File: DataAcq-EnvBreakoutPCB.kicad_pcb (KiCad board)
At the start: 2 copper layers, 19 x 41.3 mm, 22 parts, among them J1 Airflow, J2 Temp, J3 Humidity, U1 FS3000-1005, U2 LMT87DCK, U3 SHT45

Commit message: tweaking
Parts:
- removed J1: Airflow, Connector_Molex:Molex_Nano-Fit_105309-xx04_1x04_P2.50mm_Vertical
- removed J2: Temp, Connector_Molex:Molex_Nano-Fit_105309-xx03_1x03_P2.50mm_Vertical
- removed J3: Humidity, Connector_Molex:Molex_Nano-Fit_105309-xx04_1x04_P2.50mm_Vertical
- added J4: Breakout Connector, Connector_Molex:Molex_Nano-Fit_105310-xx10_2x05_P2.50mm_Vertical, B.Cu at (128.4, 38.6)
- C5, C6, R1: moved to B.Cu
- LOGO3: footprint UTSVT_Special:UTSVT_Logo_Symbol -> images:utsvt_small; moved to B.Cu
- moved LOGO3 36.3 mm to (115.8, 29.9)
- moved LOGO1 16.9 mm to (116.0, 45.4), turned to 180 degrees
- moved D2 11.7 mm to (127.2, 32.8)
- moved R3 11.7 mm to (129.5, 32.9)
- moved C3 10.3 mm to (122.4, 33.9), turned to 0 degrees
- moved C2 10.1 mm to (115.7, 33.9), turned to 0 degrees
- moved C1 7.09 mm to (117.3, 38.0), turned to -90 degrees
- moved C4 6.70 mm to (119.6, 38.0), turned to 90 degrees
- moved R2 6.62 mm to (127.2, 54.5)
- moved D1 6.62 mm to (129.4, 54.5)
- moved C6 6.53 mm to (122.4, 49.6)
- moved R1 6.53 mm to (120.2, 49.6)
- moved C5 4.88 mm to (124.2, 53.2), turned to 90 degrees
- moved H2 3.35 mm to (121.5, 29.6)
- moved C7 3.16 mm to (119.2, 44.6), turned to 90 degrees
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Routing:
- net /I2C2_SCL: track 14.2 -> 6.41 mm
- net /PA1(ADC): track 15.5 -> 9.30 mm, vias 1 -> 0
- net /I2C2_SDA: track 12.4 -> 7.48 mm, vias 1 -> 0
- net /TEMP_OUT: track 4.99 -> 2.05 mm, vias 0 -> 1
- net GNDA: track 19.5 -> 16.6 mm, vias 1 -> 2
- net Net-(D2-A): track 2.27 -> 0.00 mm
- net Net-(D1-A): track 2.26 -> 0.00 mm
- net /I2C1_SCL: track 8.22 -> 6.82 mm
- net +3.3V: track 0.00 -> 1.35 mm, vias 1 -> 2
- net /I2C1_SDA: track 9.25 -> 8.37 mm, vias 0 -> 1
- net VDDA: track 13.9 -> 14.7 mm
- net GND: vias 5 -> 4
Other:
- board size 19 x 41.3 mm -> 18.7 x 35.2 mm
- board text added: "EnvBrd Conn"
- board text removed: "Aflw"
- board text removed: "Hmdty"

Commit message: im blind
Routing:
- net Net-(D2-A): track 0.00 -> 2.27 mm
- net Net-(D1-A): track 0.00 -> 2.26 mm
- net GND: vias 4 -> 5
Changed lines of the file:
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@@
+	)
+	(via
+		(at 127.25 33.7675)
+		(size 0.6)
+		(drill 0.3)
+		(layers "F.Cu" "B.Cu")
+		(net 2)
 	)
 	(via
@@
 	)
 	(segment
+		(start 127.225 55.45)
+		(end 127.2 55.425)
+		(width 0.2)
+		(layer "B.Cu")
+		(net 10)
+	)
+	(segment
+		(start 129.45 55.45)
+		(end 127.225 55.45)
+		(width 0.2)
+		(layer "B.Cu")
+		(net 10)
+	)
+	(segment
+		(start 127.295 31.9375)
+		(end 127.25 31.8925)
+		(width 0.2)
+		(layer "B.Cu")
+		(net 11)
+	)
+	(segment
+		(start 129.5 31.9375)
+		(end 127.295 31.9375)
+		(width 0.2)
+		(layer "B.Cu")
+		(net 11)
+	)
+	(segment

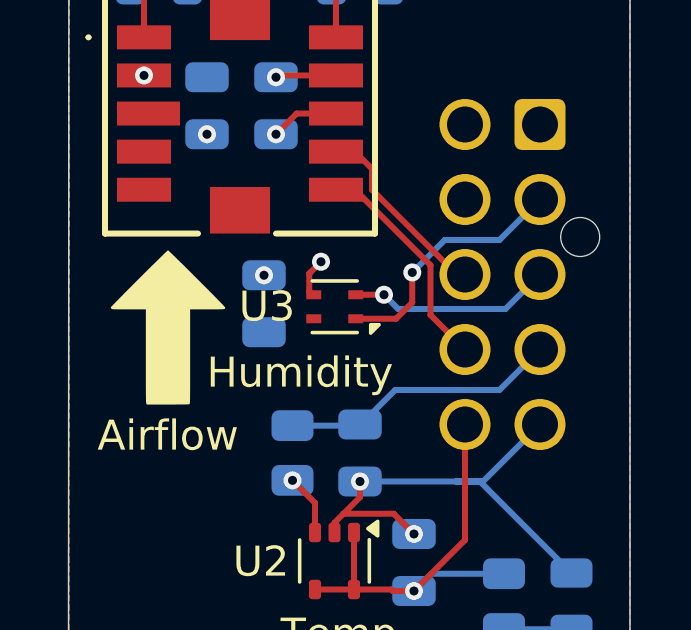
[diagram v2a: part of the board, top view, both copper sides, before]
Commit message: rearrange connector
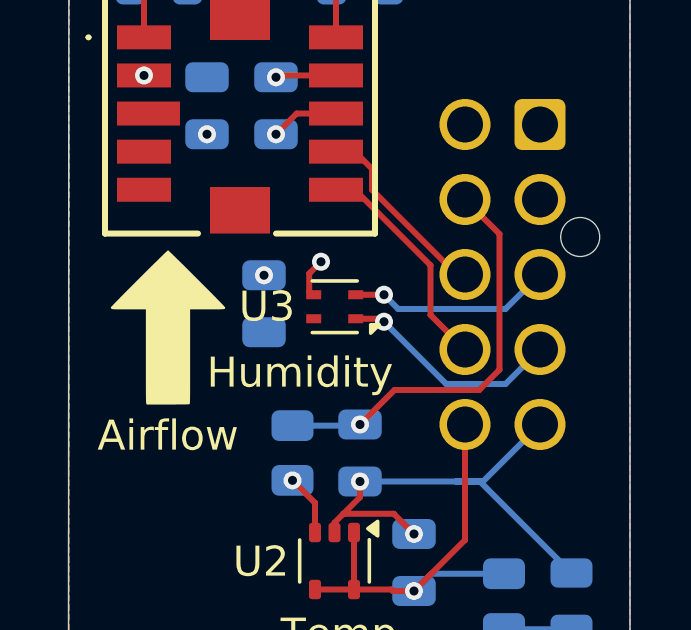
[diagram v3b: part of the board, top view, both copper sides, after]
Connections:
- J4 pad 2: /I2C1_SDA -> unconnected-(J4-Pin_2-Pad2)
- J4 pad 4: /PA1(ADC) -> /I2C1_SDA
- J4 pad 7: unconnected-(J4-Pin_7-Pad7) -> /PA1(ADC)
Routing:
- net /PA1(ADC): track 9.30 -> 13.8 mm, vias 0 -> 1
- net /I2C1_SDA: track 8.37 -> 7.52 mm
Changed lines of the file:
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@@
 	(net 19 "/I2C1_SCL")
 	(net 20 "/I2C1_SDA")
-	(net 21 "unconnected-(J4-Pin_7-Pad7)")
+	(net 21 "unconnected-(J4-Pin_2-Pad2)")
 	(footprint "Package_TO_SOT_SMD:SOT-353_SC-70-5"
 		(layer "F.Cu")
@@
 		)
 		(fp_text user "${REFERENCE}"
-			(at 0 0 360)
+			(at 0 0 0)
 			(layer "F.Fab")
 			(effects
@@
 		(tags "DFN NoLead")
 		(property "Reference" "U3"
-			(at 2.2575 0 360)
+			(at 2.2575 0 0)
 			(layer "F.SilkS")
 			(effects
@@
 		)
 		(property "Value" "SHT45"
-			(at 0 1.7 360)
+			(at 0 1.7 0)
 			(layer "F.Fab")
 			(effects
@@
 		)
 		(fp_text user "${REFERENCE}"
-			(at 0 0 360)
+			(at 0 0 0)
 			(layer "F.Fab")
 			(effects
@@
 		)
 		(property "Value" "FS3000-1005"
-			(at 0 0 360)
+			(at 0 0 0)
 			(layer "F.SilkS")
 			(hide yes)
@@
 		)
 		(property "Footprint" "SamacSys_Parts:FS30001005"
-			(at 0 0 360)
+			(at 0 0 0)
 			(layer "F.Fab")
 			(hide yes)
@@
 		)
 		(property "Datasheet" "https://www.renesas.com/us/en/document/dst/fs3000-datasheet?language=en&r=1395551"
-			(at 0 0 360)
+			(at 0 0 0)
 			(layer "F.Fab")
 			(hide yes)
@@
 		)
 		(property "Description" "The FS3000 is a surface-mount type air velocity module utilizing a MEMS thermopile-based sensor. The FS3000 features a digital output with 12-bit resolution. The sensor comprises a solid thermal isolation technology and silicon-carbide coating to protect it from abrasive wear and water condensation.The FS3000 features a compact design fit for low profile enclosures."
-			(at 0 0 360)
+			(at 0 0 0)
 			(layer "F.Fab")
 			(hide yes)
@@
 		)
 		(fp_text user "${REFERENCE}"
-			(at 0 0 360)
+			(at 0 0 0)
 			(layer "F.Fab")
 			(effects
@@
 		(at 116.00547 45.4 180)
 		(property "Reference" "LOGO1"
-			(at 0 0 360)
+			(at 0 0 0)
 			(layer "F.Fab")
 			(effects
@@
 		)
 		(property "Value" "Arrow"
-			(at 0.75 0 360)
+			(at 0.75 0 0)
 			(layer "F.SilkS")
 			(hide yes)
@@
 		)
 		(property "Footprint" "images:arrow"
-			(at 0 0 360)
+			(at 0 0 0)
 			(layer "F.Fab")
 			(hide yes)
@@
 		)
 		(property "Datasheet" ""
-			(at 0 0 360)
+			(at 0 0 0)
 			(layer "F.Fab")
 			(hide yes)
@@
 		)
 		(property "Description" "Graph footprint placeholder"
-			(at 0 0 360)
+			(at 0 0 0)
 			(layer "F.Fab")
 			(hide yes)
@@
 		)
 		(property "Value" "0.1uF"
-			(at 0 -1.68 360)
+			(at 0 -1.68 0)
 			(layer "B.Fab")
 			(effects
@@
 		)
 		(fp_text user "${REFERENCE}"
-			(at 0 0 360)
+			(at 0 0 0)
 			(layer "B.Fab")
 			(effects
@@
 		(tags "capacitor")
 		(property "Reference" "C1"
-			(at 2.5 0 360)
+			(at 2.5 0 0)
 			(layer "B.SilkS")
 			(effects
@@
 		(tags "connector Molex Nano-Fit side entry")
 		(property "Reference" "J4"
-			(at 1.25 2.92 360)
+			(at 1.25 2.92 0)
 			(layer "B.SilkS")
 			(effects
@@
 		)
 		(property "Value" "Breakout Connector"
-			(at 1.25 -12.92 360)
+			(at 1.25 -12.92 0)
 			(layer "B.Fab")
 			(effects
@@
 			)
 		)
-		(property "P/N" " 1053101110"
+		(property "P/N" "1053101110"
 			(at 0 0 0)
 			(unlocked yes)
@@
 			(layers "*.Cu" "*.Mask")
 			(remove_unused_layers no)
-			(net 20 "/I2C1_SDA")
+			(net 21 "unconnected-(J4-Pin_2-Pad2)")
 			(pinfunction "Pin_2")
-			(pintype "passive")
+			(pintype "passive+no_connect")
 		)
 		(pad "3" thru_hole circle
@@
 			(layers "*.Cu" "*.Mask")
 			(remove_unused_layers no)
-			(net 9 "/PA1(ADC)")
+			(net 20 "/I2C1_SDA")
 			(pinfunction "Pin_4")
 			(pintype "passive")
@@
 			(layers "*.Cu" "*.Mask")
 			(remove_unused_layers no)
-			(net 21 "unconnected-(J4-Pin_7-Pad7)")
+			(net 9 "/PA1(ADC)")
 			(pinfunction "Pin_7")
-			(pintype "passive+no_connect")
+			(pintype "passive")
 		)
 		(pad "8" thru_hole circle
@@
 		(tags "capacitor")
 		(property "Reference" "C4"
-			(at -2.5 -0.09 360)
+			(at -2.5 -0.09 0)
 			(layer "B.SilkS")
 			(effects
@@
 		)
 		(property "Value" "1uF"
-			(at 0 -1.68 360)
+			(at 0 -1.68 0)
 			(layer "B.Fab")
 			(effects
@@
 		)
 		(fp_text user "${REFERENCE}"
-			(at 0 0 360)
+			(at 0 0 0)
 			(layer "B.Fab")
 			(effects
@@
 	)
 	(segment
-		(start 122.425 48.625)
-		(end 123.575 47.475)
+		(start 123.55 47.475)
+		(end 122.4 48.625)
 		(width 0.2)
-		(layer "B.Cu")
+		(layer "F.Cu")
 		(net 9)
 	)
 	(segment
-		(start 120.15 48.6625)
-		(end 122.3625 48.6625)
+		(start 127.05 46.801346)
+		(end 126.376346 47.475)
 		(width 0.2)
-		(layer "B.Cu")
+		(layer "F.Cu")
 		(net 9)
 	)
 	(segment
-		(start 123.575 47.475)
-		(end 127.05 47.475)
+		(start 125.9 41.125)
+		(end 127.05 42.275)
 		(width 0.2)
-		(layer "B.Cu")
+		(layer "F.Cu")
 		(net 9)
 	)
 	(segment
-		(start 127.05 47.475)
-		(end 128.4 46.125)
+		(start 126.376346 47.475)
+		(end 123.55 47.475)
 		(width 0.2)
-		(layer "B.Cu")
+		(layer "F.Cu")
 		(net 9)
 	)
 	(segment
-		(start 122.4 48.625)
-		(end 122.425 48.625)
+		(start 127.05 42.275)
+		(end 127.05 46.801346)
+		(width 0.2)
+		(layer "F.Cu")
+		(net 9)
+	)
+	(via
+		(at 122.4 48.625)
+		(size 0.6)
+		(drill 0.3)
+		(layers "F.Cu" "B.Cu")
+		(net 9)
+	)
+	(segment
+		(start 120.15 48.6625)
+		(end 122.3625 48.6625)
 		(width 0.2)
 		(layer "B.Cu")
@@
 	)
 	(segment
-		(start 124.142892 44.557108)
-		(end 123.6 45.1)
+		(start 123.2 45.2)
+		(end 123.1 45.1)
 		(width 0.2)
 		(layer "F.Cu")
@@
 	)
 	(segment
-		(start 123.6 45.1)
+		(start 123.1 45.1)
 		(end 122.2575 45.1)
 		(width 0.2)
@@
 		(net 20)
 	)
-	(segment
-		(start 124.142892 43.557108)
-		(end 124.142892 44.557108)
-		(width 0.2)
-		(layer "F.Cu")
-		(net 20)
-	)
 	(via
-		(at 124.142892 43.557108)
+		(at 123.2 45.2)
 		(size 0.6)
 		(drill 0.3)
@@
 	)
 	(segment
-		(start 127.05 42.475)
-		(end 125.225 42.475)
+		(start 127.25 47.275)
+		(end 125.275 47.275)
 		(width 0.2)
 		(layer "B.Cu")
@@
 	)
 	(segment
-		(start 128.4 41.125)
-		(end 127.05 42.475)
+		(start 128.4 46.125)
+		(end 127.25 47.275)
 		(width 0.2)
 		(layer "B.Cu")
@@
 	)
 	(segment
-		(start 125.225 42.475)
-		(end 124.142892 43.557108)
+		(start 125.275 47.275)
+		(end 123.2 45.2)
 		(width 0.2)
 		(layer "B.Cu")

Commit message: even smaller
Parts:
- moved LOGO3 15.0 mm to (114.0, 44.8)
- moved R2 12.7 mm to (114.8, 52.0)
- moved D1 12.7 mm to (117.0, 52.0)
- moved D2 12.2 mm to (115.5, 36.3)
- moved R3 12.2 mm to (117.8, 36.3)
- moved C7 8.42 mm to (120.6, 36.3), turned to -90 degrees
- moved U3 8.34 mm to (122.4, 36.4)
- moved H1 7.04 mm to (127.0, 53.8)
- moved H2 6.69 mm to (127.0, 33.4)
- moved C3 5.79 mm to (120.6, 39.4), turned to 180 degrees
- moved LOGO1 5.60 mm to (115.8, 51.0)
- moved C2 5.55 mm to (115.1, 39.4)
- moved U1 5.55 mm to (117.8, 43.8)
- moved C1 5.55 mm to (116.7, 43.5)
- moved C4 5.55 mm to (119.0, 43.5)
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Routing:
- net /I2C1_SDA: track 7.52 -> 12.0 mm
- net /I2C1_SCL: track 6.82 -> 10.3 mm, vias 1 -> 0
- net /I2C2_SDA: track 7.48 -> 4.98 mm
- net +3.3V: track 1.35 -> 3.49 mm
- net VDDA: track 14.7 -> 16.5 mm, vias 1 -> 2
- net GNDA: track 16.6 -> 14.9 mm
- net /TEMP_OUT: track 2.05 -> 1.39 mm
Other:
- board size 18.7 x 35.2 mm -> 19.4 x 27.2 mm
- board text removed: "EnvBrd Conn"
